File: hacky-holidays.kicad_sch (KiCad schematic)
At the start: 39 parts, among them Q1 AO3401A, Q2 AO3400A, Q3 AO3400A, SW1 SW_Push, SW2 SW_Push, SW3 SW_Push, SW4 SW_SPDT, U1 TP4057, U2 CH552G, U3 DW01A

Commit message: update capacitor part numbers, add test pins, silkscreen updates
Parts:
- added J1: Conn_01x04_Pin, Connector_PinHeader_2.54mm:PinHeader_1x04_P2.54mm_Vertical, symbol Connector:Conn_01x04_Pin
- added R4: 220, Resistor_SMD:R_0603_1608Metric, symbol Device:R
- BT3, BT9: LCSC (none) -> C2979167
- C1, C6: footprint Capacitor_SMD:C_0402_1005Metric -> Capacitor_SMD:C_0603_1608Metric; LCSC (none) -> C19702
- C2, C4, C5, C7: footprint Capacitor_SMD:C_0402_1005Metric -> Capacitor_SMD:C_0603_1608Metric; LCSC (none) -> C14663
- C3: footprint Capacitor_SMD:C_0402_1005Metric -> Capacitor_SMD:C_0603_1608Metric; LCSC (none) -> C15849
- D1, D10, D11, D2, D4, D5, D7, D8: LCSC (none) -> C22461793
- D3: LCSC (none) -> C78395
- D6: LCSC (none) -> C191023
- D9: LCSC (none) -> C84256
- Q1: LCSC (none) -> C15127
- Q2, Q3: LCSC (none) -> C20917
- R1: LCSC (none) -> C25104
- R10: LCSC (none) -> C17901
- R11, R2: LCSC (none) -> C11702
- R3: LCSC (none) -> C22967
- R8: LCSC (none) -> C25741
- R9: footprint Resistor_SMD:R_0402_1005Metric -> Resistor_SMD:R_0805_2012Metric; LCSC (none) -> C17414
- SW1: LCSC (none) -> C318884
- SW4: LCSC (none) -> C92657; now left out of the parts list
- U1: LCSC (none) -> C12044
- U2: LCSC (none) -> C111292
- U3: LCSC (none) -> C18164398
- USB1: LCSC (none) -> C36936538
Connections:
- net +3.3V: now also J1.2 (Pin_2)
- net BTN1: now also U2.7 (P3.1/PWM2_/TXD); no longer U2.11 (P3.4/PWM2/RXD1_/T0)
- net BTN2: now also U2.2 (P1.4/T2_/CAP1_/SCS/TIN2/UCC1/AIN1); no longer U2.5 (P1.7/SCK/TXD1/TIN5)
- net BUZ: now also U2.3 (P1.5/MOSI/PWM1/TIN3/UCC2/AIN2), J1.3 (Pin_3), R4.1; no longer BZ6.1 (+), U2.8 (P3.0/PWM1_/RXD)
- net GND: now also J1.4 (Pin_4)
- net WS2812B: now also D1.4 (DIN), R1.2, J1.1 (Pin_1); no longer R1.1, U2.10 (P3.3/INT1)
- net at U2.9 (P1.1/T2EX/CAP2/TIN1/VBUS2/AIN0): now also R1.1
- new net: BZ6.1 (+), R4.2
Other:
- note added: "C14663"
- note added: "C15849"
- note added: "C19702"
- note added: "TEST PINS"
- note removed: "C1525"
- note removed: "C15525"
- note removed: "C52923"
- moved on the sheet: BZ6, R1

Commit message: tidy schematic
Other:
- note added: "Bootloader"
- note removed: "Bootloader C25744"
- note removed: "C11702"
- note removed: "C14663"
- note removed: "C15849"
- note removed: "C17901"
- note removed: "C19702"
- note removed: "C22967"
- note removed: "C25104"
- note removed: "C25741"
- note removed: "C2979167"
- note removed: "C36936538"
- moved on the sheet: D9

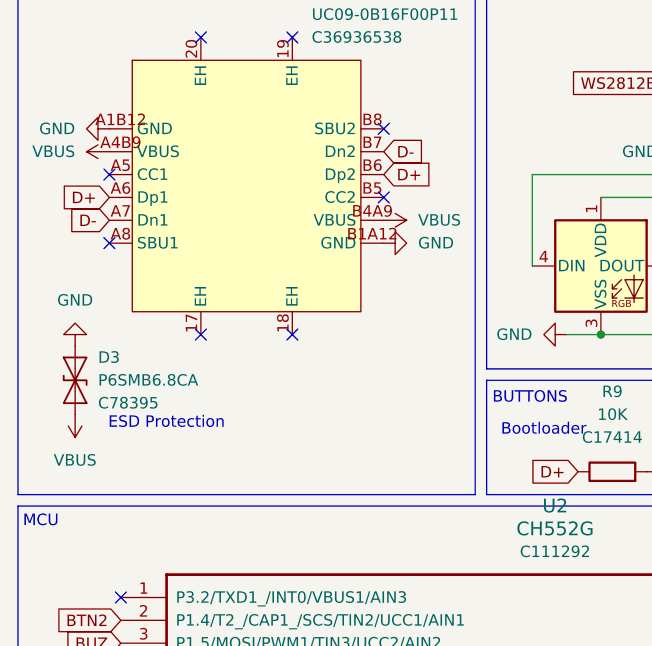
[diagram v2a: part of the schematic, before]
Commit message: add usb cc resistors
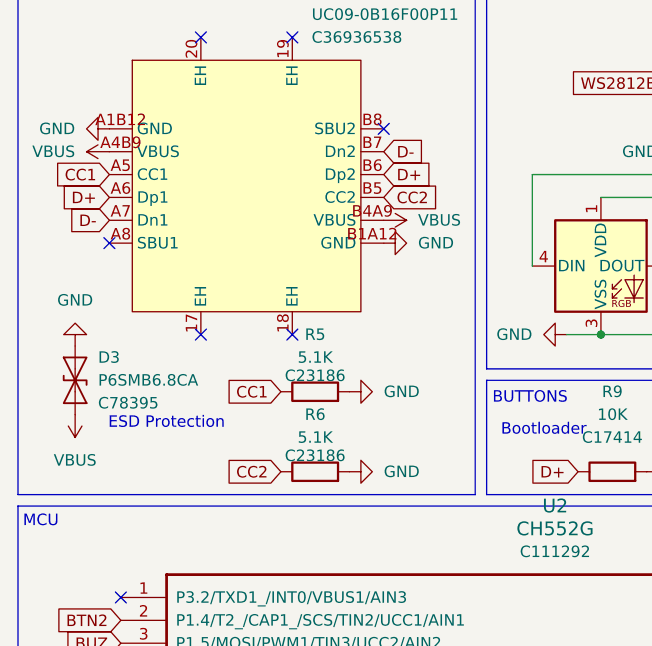
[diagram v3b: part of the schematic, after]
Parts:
- added R5, R6: 5.1K, Resistor_SMD:R_0603_1608Metric, symbol Device:R
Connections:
- net GND: now also R5.2, R6.2
- net CC1: now reaches USB1.A5 (CC1)
- net CC1: now also R5.1
- net CC2: now reaches USB1.B5 (CC2)
- net CC2: now also R6.1
- no-connect marks 17 -> 15

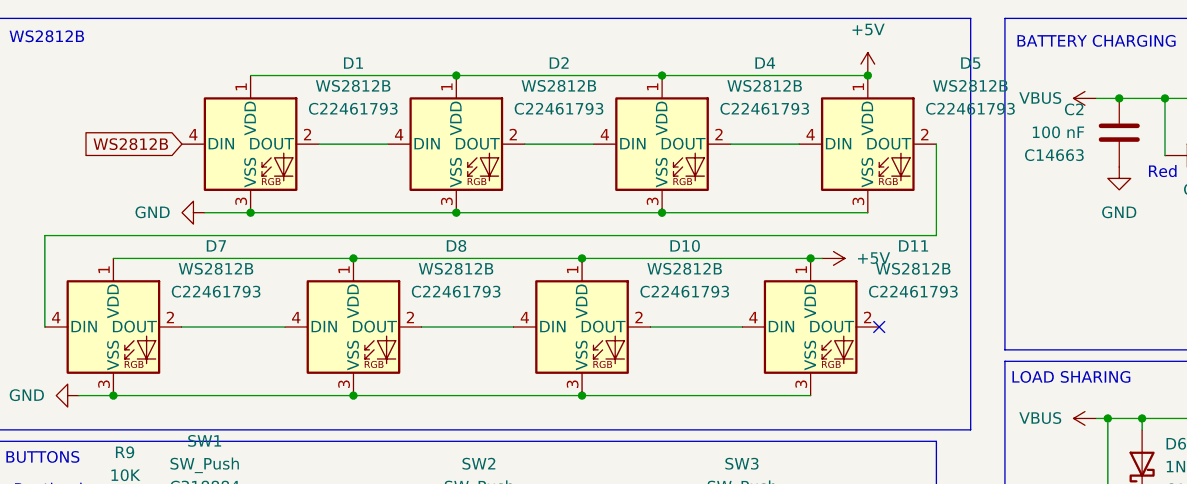
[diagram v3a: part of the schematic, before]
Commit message: use economic ws2812bs
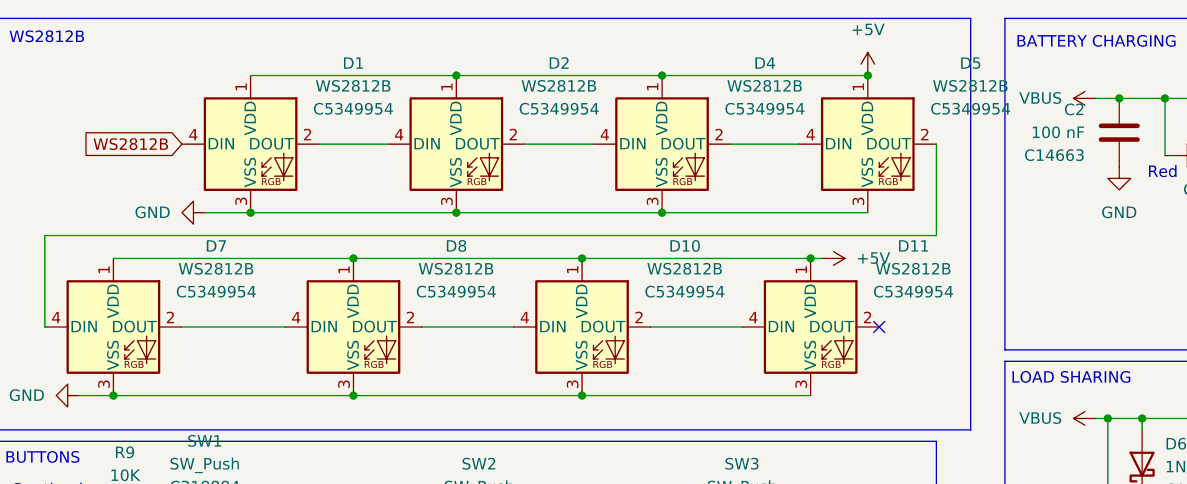
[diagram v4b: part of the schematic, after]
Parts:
- D1, D10, D11, D2, D4, D5, D7, D8: footprint LED_SMD:LED_WS2812B_PLCC4_5.0x5.0mm_P3.2mm -> lcsc-imports:LED-SMD_4P-L1.6-W1.5_XL-1615RGBC-WS2812B; LCSC C22461793 -> C5349954
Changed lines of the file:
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@@
 			)
 		)
-		(property "Footprint" "LED_SMD:LED_WS2812B_PLCC4_5.0x5.0mm_P3.2mm"
+		(property "Footprint" "lcsc-imports:LED-SMD_4P-L1.6-W1.5_XL-1615RGBC-WS2812B"
 			(at 95.25 35.56 0)
 			(effects
@@
 			)
 		)
-		(property "LCSC" "C22461793"
+		(property "LCSC" "C5349954"
 			(at 105.41 24.0598 0)
 			(effects
@@
 			)
 		)
-		(property "Footprint" "LED_SMD:LED_WS2812B_PLCC4_5.0x5.0mm_P3.2mm"
+		(property "Footprint" "lcsc-imports:LED-SMD_4P-L1.6-W1.5_XL-1615RGBC-WS2812B"
 			(at 118.11 35.56 0)
 			(effects
@@
 			)
 		)
-		(property "LCSC" "C22461793"
+		(property "LCSC" "C5349954"
 			(at 128.27 24.0598 0)
 			(effects
@@
 			)
 		)
-		(property "Footprint" "LED_SMD:LED_WS2812B_PLCC4_5.0x5.0mm_P3.2mm"
+		(property "Footprint" "lcsc-imports:LED-SMD_4P-L1.6-W1.5_XL-1615RGBC-WS2812B"
 			(at 132.08 55.88 0)
 			(effects
@@
 			)
 		)
-		(property "LCSC" "C22461793"
+		(property "LCSC" "C5349954"
 			(at 142.24 44.3798 0)
 			(effects
@@
 			)
 		)
-		(property "Footprint" "LED_SMD:LED_WS2812B_PLCC4_5.0x5.0mm_P3.2mm"
+		(property "Footprint" "lcsc-imports:LED-SMD_4P-L1.6-W1.5_XL-1615RGBC-WS2812B"
 			(at 106.68 55.88 0)
 			(effects
@@
 			)
 		)
-		(property "LCSC" "C22461793"
+		(property "LCSC" "C5349954"
 			(at 116.84 44.3798 0)
 			(effects
@@
 			)
 		)
-		(property "Footprint" "LED_SMD:LED_WS2812B_PLCC4_5.0x5.0mm_P3.2mm"
+		(property "Footprint" "lcsc-imports:LED-SMD_4P-L1.6-W1.5_XL-1615RGBC-WS2812B"
 			(at 80.01 55.88 0)
 			(effects
@@
 			)
 		)
-		(property "LCSC" "C22461793"
+		(property "LCSC" "C5349954"
 			(at 90.17 44.3798 0)
 			(effects
@@
 			)
 		)
-		(property "Footprint" "LED_SMD:LED_WS2812B_PLCC4_5.0x5.0mm_P3.2mm"
+		(property "Footprint" "lcsc-imports:LED-SMD_4P-L1.6-W1.5_XL-1615RGBC-WS2812B"
 			(at 163.83 35.56 0)
 			(effects
@@
 			)
 		)
-		(property "LCSC" "C22461793"
+		(property "LCSC" "C5349954"
 			(at 173.99 24.0598 0)
 			(effects
@@
 			)
 		)
-		(property "Footprint" "LED_SMD:LED_WS2812B_PLCC4_5.0x5.0mm_P3.2mm"
+		(property "Footprint" "lcsc-imports:LED-SMD_4P-L1.6-W1.5_XL-1615RGBC-WS2812B"
 			(at 140.97 35.56 0)
 			(effects
@@
 			)
 		)
-		(property "LCSC" "C22461793"
+		(property "LCSC" "C5349954"
 			(at 151.13 24.0598 0)
 			(effects
@@
 			)
 		)
-		(property "Footprint" "LED_SMD:LED_WS2812B_PLCC4_5.0x5.0mm_P3.2mm"
+		(property "Footprint" "lcsc-imports:LED-SMD_4P-L1.6-W1.5_XL-1615RGBC-WS2812B"
 			(at 157.48 55.88 0)
 			(effects
@@
 			)
 		)
-		(property "LCSC" "C22461793"
+		(property "LCSC" "C5349954"
 			(at 167.64 44.3798 0)
 			(effects
